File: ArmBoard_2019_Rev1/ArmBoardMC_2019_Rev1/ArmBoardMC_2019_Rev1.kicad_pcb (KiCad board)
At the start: 2 copper layers, 58 parts, among them U1 VNH5019A_E, U10 Limit_Switch7, U11 Limit_Switch2, U12 Limit_Switch4, U13 Limit_Switch6, U14 Limit_Switch8, U15 MAX_3232, U16 OKI, U17 Encoder_1, U18 Encoder_3, U19 Encoder_2, U2 VNH5019A_E, U20 Encoder_4, U3 TM4C129E_Launchpad, U5 VNH5019A_E, U6 VNH5019A_E, U7 Limit_Switch1, U8 Limit_Switch3, U9 Limit_Switch5

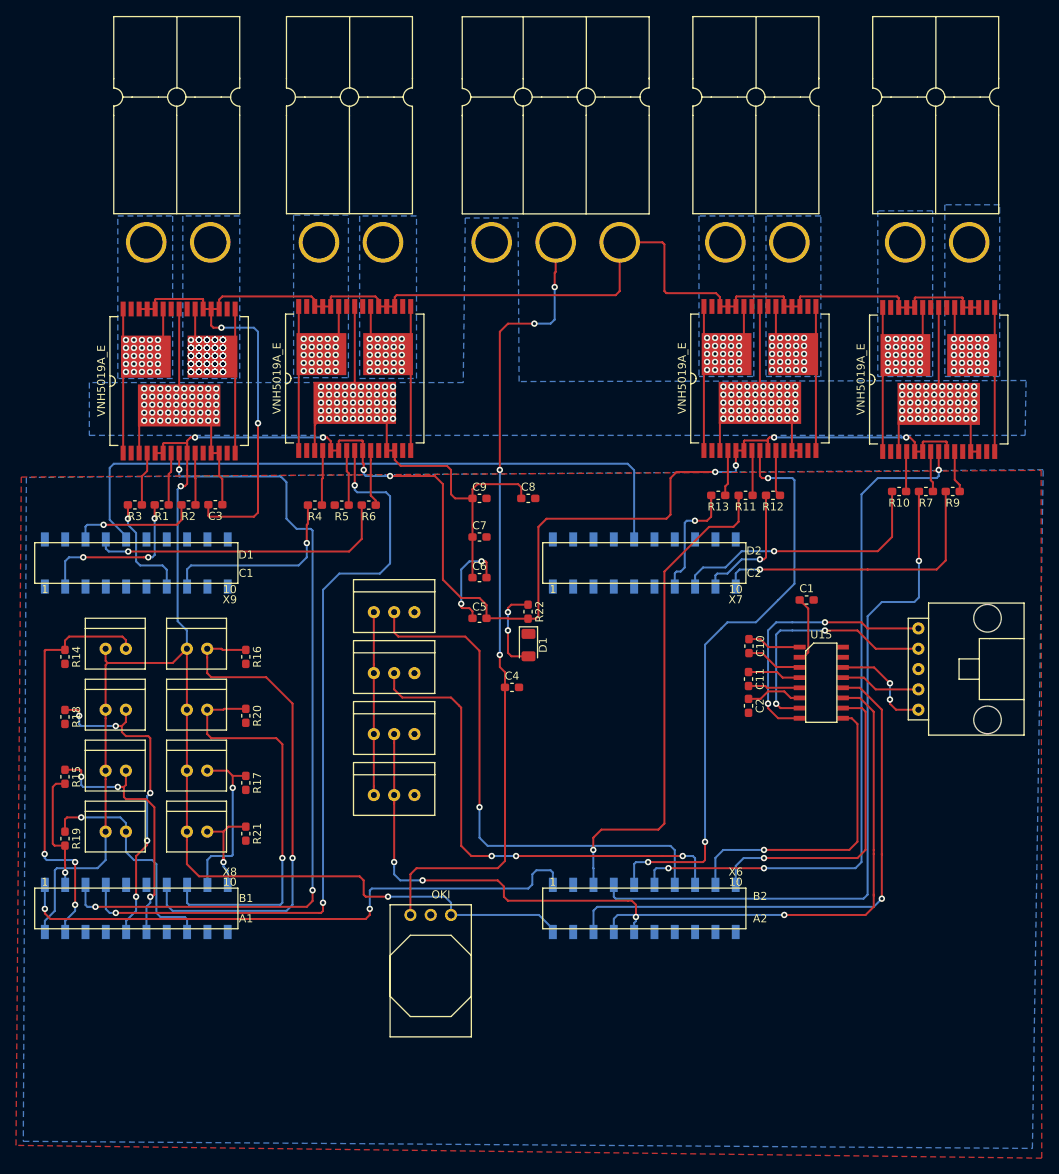
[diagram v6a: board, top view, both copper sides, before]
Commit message: Made some changes to board wiring
changed from 9.84 mil wire to 15.00 mil wire and changed some of the routing to be more efficient and clean
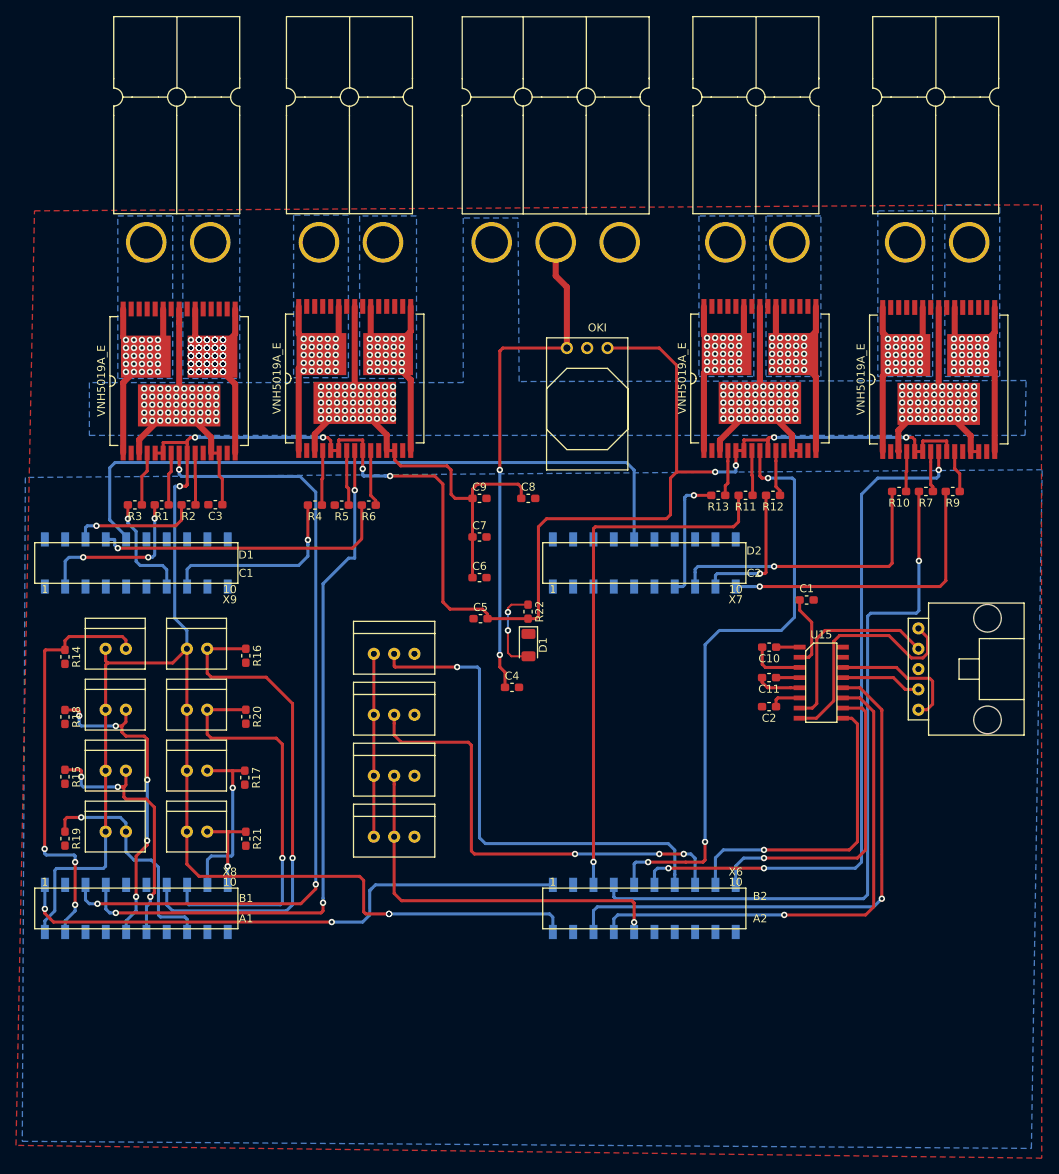
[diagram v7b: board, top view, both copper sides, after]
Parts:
- moved U16 73.5 mm to (103.9, 65.5)
- moved U17 5.21 mm to (79.8, 102.5)
- moved U20 5.21 mm to (79.8, 125.3)
- moved U18 5.21 mm to (79.8, 117.7)
- moved U19 5.21 mm to (79.8, 110.1)
- moved C11 2.57 mm to (131.7, 108.0), turned to 180 degrees
- moved C2 2.57 mm to (131.7, 111.6), turned to 180 degrees
- moved C10 2.53 mm to (131.7, 104.2), turned to 180 degrees
- moved R17 0.66 mm to (66.2, 120.5)
- moved R21 0.64 mm to (66.3, 128.1)
- moved R16 0.14 mm to (66.3, 105.3)
- moved C5 0.14 mm to (95.6, 100.6)
- moved R20 0.11 mm to (66.3, 112.9)
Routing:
- net GND: track 201.2 -> 0.00 mm, vias 5 -> 0
- net Logic_3.3V: track 307.7 -> 355.1 mm, vias 10 -> 11
- net /V+Log: track 101.2 -> 64.6 mm, vias 4 -> 2
- net I_Sense_2: track 98.4 -> 129.3 mm
- net RX_1_Tiva: track 69.1 -> 92.7 mm
- net Encoder3_PWM: track 54.5 -> 64.3 mm, vias 3 -> 1
- net TX_2_SL: track 30.8 -> 24.6 mm, vias 2 -> 0
- net LS_2: track 41.2 -> 46.1 mm
- net /Out_A1: track 29.7 -> 25.1 mm
- net /Out_B1: track 28.8 -> 24.4 mm
- net RX_2_SL: track 33.7 -> 29.6 mm, vias 2 -> 0
- net Net-(C11-Pad1): track 6.95 -> 2.95 mm
- net Encoder2_PWM: track 61.8 -> 58.0 mm
- net Net-(C10-Pad1): track 6.76 -> 2.94 mm
- net MOTOR3_PWM: track 62.7 -> 66.5 mm
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
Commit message: Revert "Made some changes to board wiring"
This reverts commit da9662cbcf42a8357acbb6e05bfca608f18f2124.
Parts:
- moved U16 73.5 mm to (84.3, 136.4)
- moved U17 5.21 mm to (79.8, 97.3)
- moved U20 5.21 mm to (79.8, 120.1)
- moved U18 5.21 mm to (79.8, 112.5)
- moved U19 5.21 mm to (79.8, 104.9)
- moved C11 2.57 mm to (129.1, 108.2), turned to 270 degrees
- moved C2 2.57 mm to (129.1, 111.5), turned to 270 degrees
- moved C10 2.53 mm to (129.2, 104.1), turned to 270 degrees
- moved R17 0.66 mm to (66.3, 121.2)
- moved R21 0.64 mm to (66.3, 127.5)
- moved R16 0.14 mm to (66.3, 105.4)
- moved C5 0.14 mm to (95.5, 100.6)
- moved R20 0.11 mm to (66.3, 112.8)
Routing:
- net GND: track 0.00 -> 201.2 mm, vias 0 -> 5
- net Logic_3.3V: track 355.1 -> 307.7 mm, vias 11 -> 10
- net /V+Log: track 64.6 -> 101.2 mm, vias 2 -> 4
- net I_Sense_2: track 129.3 -> 98.4 mm
- net RX_1_Tiva: track 92.7 -> 69.1 mm
- net Encoder3_PWM: track 64.3 -> 54.5 mm, vias 1 -> 3
- net TX_2_SL: track 24.6 -> 30.8 mm, vias 0 -> 2
- net LS_2: track 46.1 -> 41.2 mm
- net /Out_A1: track 25.1 -> 29.7 mm
- net /Out_B1: track 24.4 -> 28.8 mm
- net RX_2_SL: track 29.6 -> 33.7 mm, vias 0 -> 2
- net Net-(C11-Pad1): track 2.95 -> 6.95 mm
- net Encoder2_PWM: track 58.0 -> 61.8 mm
- net Net-(C10-Pad1): track 2.94 -> 6.76 mm
- net MOTOR3_PWM: track 66.5 -> 62.7 mm
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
